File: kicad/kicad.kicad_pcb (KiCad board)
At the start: 2 copper layers, 86.4 x 53.3 mm, 12 parts, among them J1 Conn_01x06_Male, J2 Conn_01x02_Male, J3 Conn_01x02_Male, U1 4Bit_China_Level_Shifter, U2 WeMos_D1_mini, U3 LTV-817

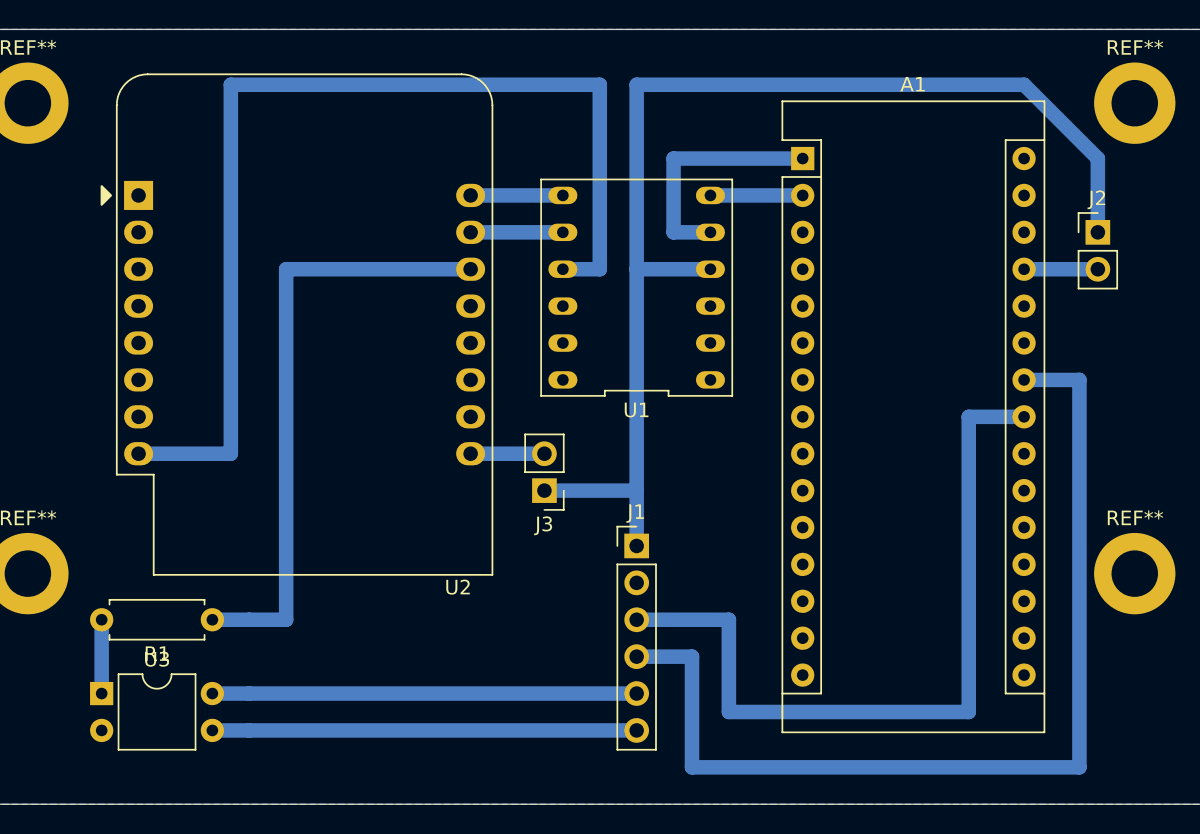
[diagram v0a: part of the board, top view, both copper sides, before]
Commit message: make thicker wires to make soldering of routed pcbs easier
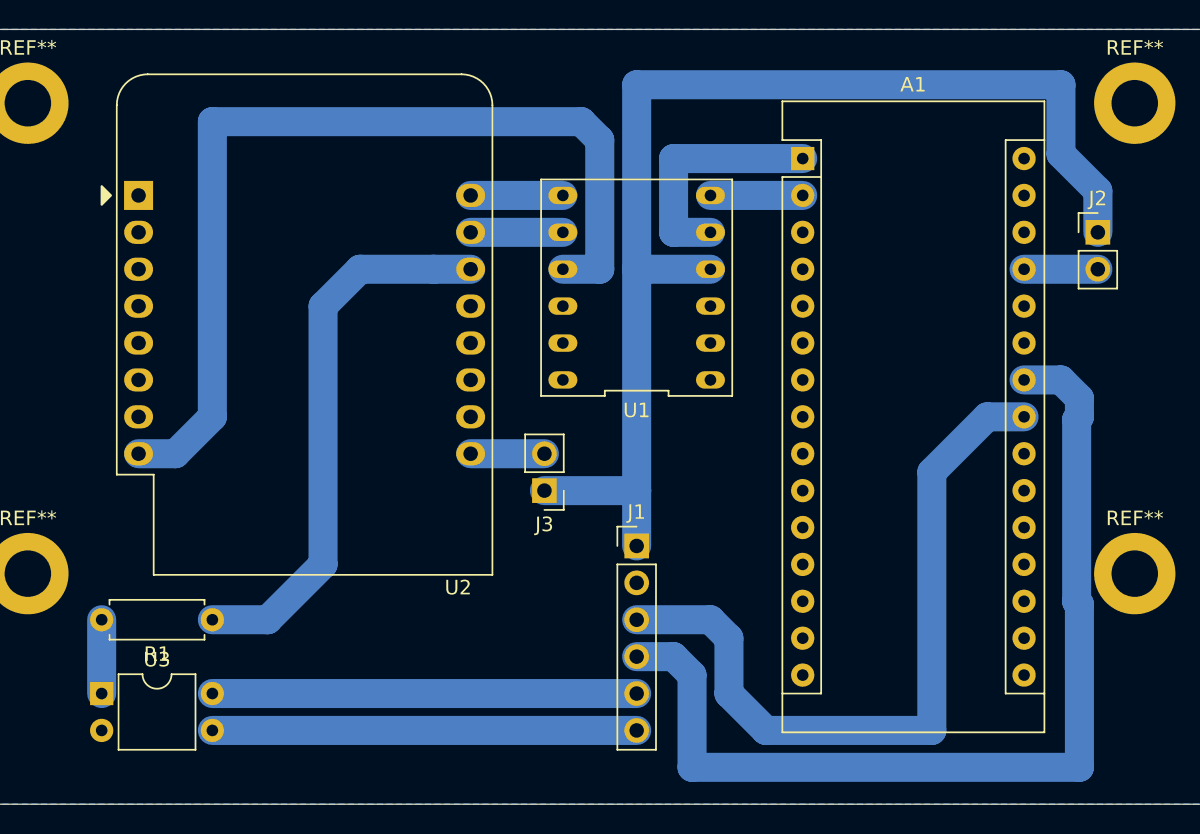
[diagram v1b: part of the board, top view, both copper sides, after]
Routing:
- net Net-(U1-Pad9): track 72.4 -> 65.1 mm
- net Net-(R1-Pad1): track 41.9 -> 38.2 mm
- net SDA: track 53.3 -> 51.4 mm
- net VCC: track 82.1 -> 83.6 mm
- net SCL: track 68.6 -> 67.2 mm
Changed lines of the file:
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@@
     (thickness 1.6)
     (drawings 4)
-    (tracks 40)
+    (tracks 52)
     (zones 0)
     (modules 12)
@@
   )
   (setup
-    (last_trace_width 1)
+    (last_trace_width 2)
     (user_trace_width 1)
+    (user_trace_width 2)
     (trace_clearance 0.2)
     (zone_clearance 0.508)
@@
   (gr_line (start 134.62 48.26) (end 134.62 101.6) (layer Edge.Cuts) (width 0.05))
   (gr_line (start 48.26 48.26) (end 134.62 48.26) (layer Edge.Cuts) (width 0.05))
-  (segment (start 100.33 62.23) (end 97.79 62.23) (width 1) (layer B.Cu) (net 1))
-  (segment (start 97.79 62.23) (end 97.79 57.15) (width 1) (layer B.Cu) (net 1))
-  (segment (start 97.79 57.15) (end 106.68 57.15) (width 1) (layer B.Cu) (net 1))
-  (segment (start 100.33 59.69) (end 106.68 59.69) (width 1) (layer B.Cu) (net 3))
-  (segment (start 118.11 74.93) (end 121.92 74.93) (width 1) (layer B.Cu) (net 13))
-  (segment (start 118.11 95.25) (end 118.11 74.93) (width 1) (layer B.Cu) (net 13))
-  (segment (start 101.6 95.25) (end 118.11 95.25) (width 1) (layer B.Cu) (net 13))
-  (segment (start 101.6 88.9) (end 101.6 95.25) (width 1) (layer B.Cu) (net 13))
-  (segment (start 95.25 88.9) (end 101.6 88.9) (width 1) (layer B.Cu) (net 13))
-  (segment (start 125.73 72.39) (end 121.92 72.39) (width 1) (layer B.Cu) (net 14))
-  (segment (start 125.73 99.06) (end 125.73 72.39) (width 1) (layer B.Cu) (net 14))
-  (segment (start 99.06 99.06) (end 125.73 99.06) (width 1) (layer B.Cu) (net 14))
-  (segment (start 99.06 91.44) (end 99.06 99.06) (width 1) (layer B.Cu) (net 14))
-  (segment (start 95.25 91.44) (end 99.06 91.44) (width 1) (layer B.Cu) (net 14))
-  (segment (start 127 64.77) (end 121.92 64.77) (width 1) (layer B.Cu) (net 20))
-  (segment (start 88.9 80.01) (end 95.25 80.01) (width 1) (layer B.Cu) (net 28))
-  (segment (start 95.25 80.01) (end 95.25 83.82) (width 1) (layer B.Cu) (net 28))
-  (segment (start 95.25 52.07) (end 121.92 52.07) (width 1) (layer B.Cu) (net 28))
-  (segment (start 121.92 52.07) (end 127 57.15) (width 1) (layer B.Cu) (net 28))
-  (segment (start 127 57.15) (end 127 62.23) (width 1) (layer B.Cu) (net 28))
-  (segment (start 95.25 64.77) (end 100.33 64.77) (width 1) (layer B.Cu) (net 28))
-  (segment (start 95.25 80.01) (end 95.25 64.77) (width 1) (layer B.Cu) (net 28))
-  (segment (start 95.25 64.77) (end 95.25 52.07) (width 1) (layer B.Cu) (net 28))
-  (segment (start 68.58 93.98) (end 95.25 93.98) (width 1) (layer B.Cu) (net 29))
-  (segment (start 68.58 93.98) (end 66.04 93.98) (width 1) (layer B.Cu) (net 29))
-  (segment (start 68.58 96.52) (end 95.25 96.52) (width 1) (layer B.Cu) (net 30))
-  (segment (start 68.58 96.52) (end 66.04 96.52) (width 1) (layer B.Cu) (net 30))
-  (segment (start 83.82 77.47) (end 88.9 77.47) (width 1) (layer B.Cu) (net 31))
-  (segment (start 68.58 88.9) (end 71.12 88.9) (width 1) (layer B.Cu) (net 32))
-  (segment (start 71.12 88.9) (end 71.12 64.77) (width 1) (layer B.Cu) (net 32))
-  (segment (start 71.12 64.77) (end 83.82 64.77) (width 1) (layer B.Cu) (net 32))
-  (segment (start 68.58 88.9) (end 66.04 88.9) (width 1) (layer B.Cu) (net 32))
-  (segment (start 58.42 88.9) (end 58.42 93.98) (width 1) (layer B.Cu) (net 33))
-  (segment (start 90.17 64.77) (end 92.71 64.77) (width 1) (layer B.Cu) (net 38))
-  (segment (start 92.71 64.77) (end 92.71 52.07) (width 1) (layer B.Cu) (net 38))
-  (segment (start 92.71 52.07) (end 67.31 52.07) (width 1) (layer B.Cu) (net 38))
-  (segment (start 67.31 52.07) (end 67.31 77.47) (width 1) (layer B.Cu) (net 38))
-  (segment (start 67.31 77.47) (end 60.96 77.47) (width 1) (layer B.Cu) (net 38))
-  (segment (start 90.17 62.23) (end 83.82 62.23) (width 1) (layer B.Cu) (net 39))
-  (segment (start 90.17 59.69) (end 83.82 59.69) (width 1) (layer B.Cu) (net 40))
+  (segment (start 100.33 62.23) (end 97.79 62.23) (width 2) (layer B.Cu) (net 1))
+  (segment (start 97.79 62.23) (end 97.79 57.15) (width 2) (layer B.Cu) (net 1))
+  (segment (start 97.79 57.15) (end 106.68 57.15) (width 2) (layer B.Cu) (net 1))
+  (segment (start 100.33 59.69) (end 106.68 59.69) (width 2) (layer B.Cu) (net 3))
+  (segment (start 119.38 74.93) (end 121.92 74.93) (width 2) (layer B.Cu) (net 13))
+  (segment (start 115.57 78.74) (end 119.38 74.93) (width 2) (layer B.Cu) (net 13))
+  (segment (start 104.14 96.52) (end 115.57 96.52) (width 2) (layer B.Cu) (net 13))
+  (segment (start 101.6 93.98) (end 104.14 96.52) (width 2) (layer B.Cu) (net 13))
+  (segment (start 100.33 88.9) (end 101.6 90.17) (width 2) (layer B.Cu) (net 13))
+  (segment (start 115.57 96.52) (end 115.57 78.74) (width 2) (layer B.Cu) (net 13))
+  (segment (start 101.6 90.17) (end 101.6 93.98) (width 2) (layer B.Cu) (net 13))
+  (segment (start 95.25 88.9) (end 100.33 88.9) (width 2) (layer B.Cu) (net 13))
+  (segment (start 95.25 91.44) (end 97.79 91.44) (width 2) (layer B.Cu) (net 14))
+  (segment (start 121.92 72.39) (end 124.46 72.39) (width 2) (layer B.Cu) (net 14))
+  (segment (start 97.79 91.44) (end 99.06 92.71) (width 2) (layer B.Cu) (net 14))
+  (segment (start 99.06 92.71) (end 99.06 99.06) (width 2) (layer B.Cu) (net 14))
+  (segment (start 99.06 99.06) (end 125.73 99.06) (width 2) (layer B.Cu) (net 14))
+  (segment (start 125.539999 87.645001) (end 125.539999 75.120001) (width 2) (layer B.Cu) (net 14))
+  (segment (start 125.73 87.835002) (end 125.539999 87.645001) (width 2) (layer B.Cu) (net 14))
+  (segment (start 125.73 99.06) (end 125.73 87.835002) (width 2) (layer B.Cu) (net 14))
+  (segment (start 125.539999 75.120001) (end 125.73 74.93) (width 2) (layer B.Cu) (net 14))
+  (segment (start 125.73 73.66) (end 124.46 72.39) (width 2) (layer B.Cu) (net 14))
+  (segment (start 125.73 74.93) (end 125.73 73.66) (width 2) (layer B.Cu) (net 14))
+  (segment (start 127 64.77) (end 121.92 64.77) (width 2) (layer B.Cu) (net 20))
+  (segment (start 88.9 80.01) (end 95.25 80.01) (width 2) (layer B.Cu) (net 28))
+  (segment (start 95.25 83.82) (end 95.25 80.01) (width 2) (layer B.Cu) (net 28))
+  (segment (start 100.33 64.77) (end 95.25 64.77) (width 2) (layer B.Cu) (net 28))
+  (segment (start 95.25 64.77) (end 95.25 52.07) (width 2) (layer B.Cu) (net 28))
+  (segment (start 95.25 80.01) (end 95.25 64.77) (width 2) (layer B.Cu) (net 28))
+  (segment (start 127 59.38) (end 124.46 56.84) (width 2) (layer B.Cu) (net 28))
+  (segment (start 127 62.23) (end 127 59.38) (width 2) (layer B.Cu) (net 28))
+  (segment (start 124.46 56.84) (end 124.46 52.07) (width 2) (layer B.Cu) (net 28))
+  (segment (start 124.46 52.07) (end 95.25 52.07) (width 2) (layer B.Cu) (net 28))
+  (segment (start 66.04 93.98) (end 95.25 93.98) (width 2) (layer B.Cu) (net 29))
+  (segment (start 66.04 96.52) (end 95.25 96.52) (width 2) (layer B.Cu) (net 30))
+  (segment (start 83.82 77.47) (end 88.9 77.47) (width 2) (layer B.Cu) (net 31))
+  (segment (start 76.2 64.77) (end 81.28 64.77) (width 2) (layer B.Cu) (net 32))
+  (segment (start 73.66 67.31) (end 76.2 64.77) (width 2) (layer B.Cu) (net 32))
+  (segment (start 81.28 64.77) (end 83.82 64.77) (width 2) (layer B.Cu) (net 32))
+  (segment (start 73.66 85.09) (end 73.66 67.31) (width 2) (layer B.Cu) (net 32))
+  (segment (start 69.85 88.9) (end 73.66 85.09) (width 2) (layer B.Cu) (net 32))
+  (segment (start 66.04 88.9) (end 69.85 88.9) (width 2) (layer B.Cu) (net 32))
+  (segment (start 58.42 88.9) (end 58.42 93.98) (width 2) (layer B.Cu) (net 33))
+  (segment (start 63.5 77.47) (end 60.96 77.47) (width 2) (layer B.Cu) (net 38))
+  (segment (start 92.71 55.88) (end 91.44 54.61) (width 2) (layer B.Cu) (net 38))
+  (segment (start 92.71 64.77) (end 92.71 55.88) (width 2) (layer B.Cu) (net 38))
+  (segment (start 66.04 74.93) (end 63.5 77.47) (width 2) (layer B.Cu) (net 38))
+  (segment (start 66.04 54.61) (end 66.04 74.93) (width 2) (layer B.Cu) (net 38))
+  (segment (start 91.44 54.61) (end 66.04 54.61) (width 2) (layer B.Cu) (net 38))
+  (segment (start 90.17 64.77) (end 92.71 64.77) (width 2) (layer B.Cu) (net 38))
+  (segment (start 83.82 62.23) (end 90.17 62.23) (width 2) (layer B.Cu) (net 39))
+  (segment (start 90.17 59.69) (end 83.82 59.69) (width 2) (layer B.Cu) (net 40))
   (zone (net 7) (net_name GND) (layer B.Cu) (hatch edge 0.508)
     (connect_pads (clearance 0.508))

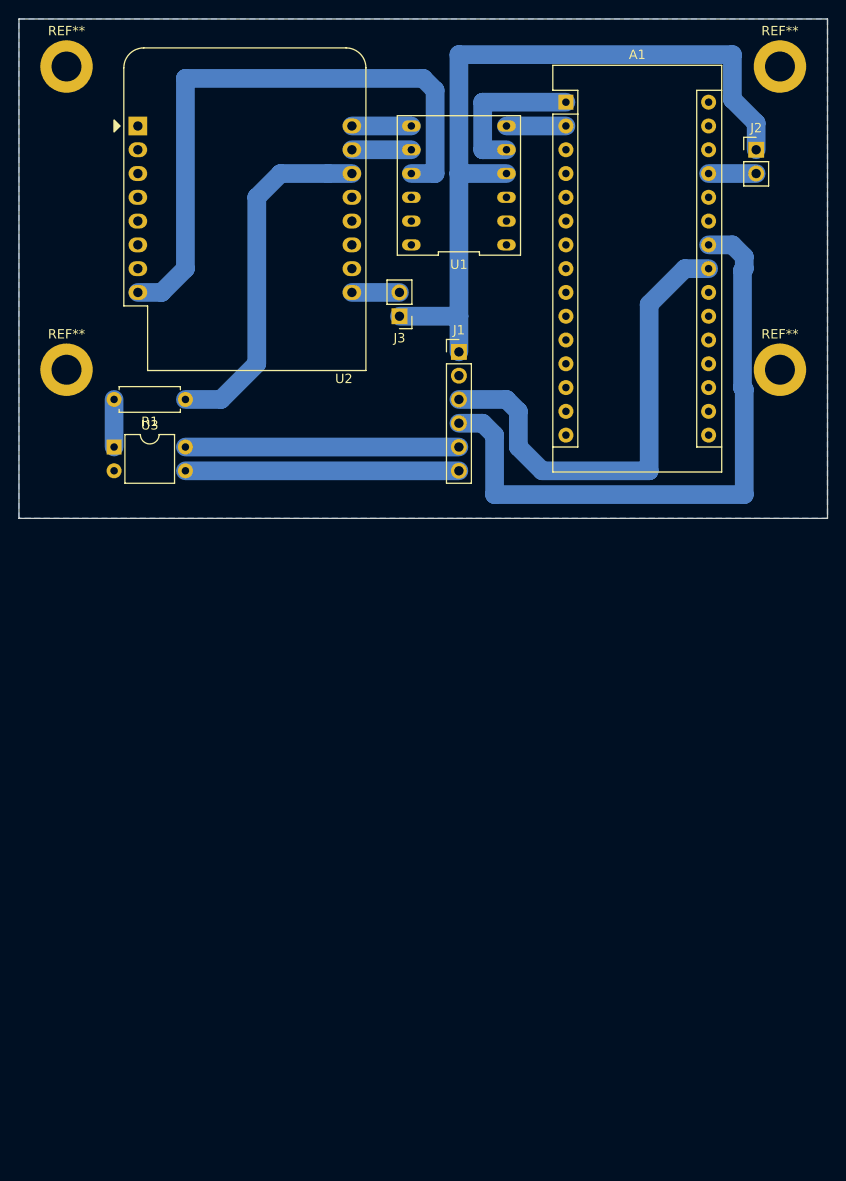
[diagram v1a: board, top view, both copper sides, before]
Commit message: add output to switch an external relay with an external voltage
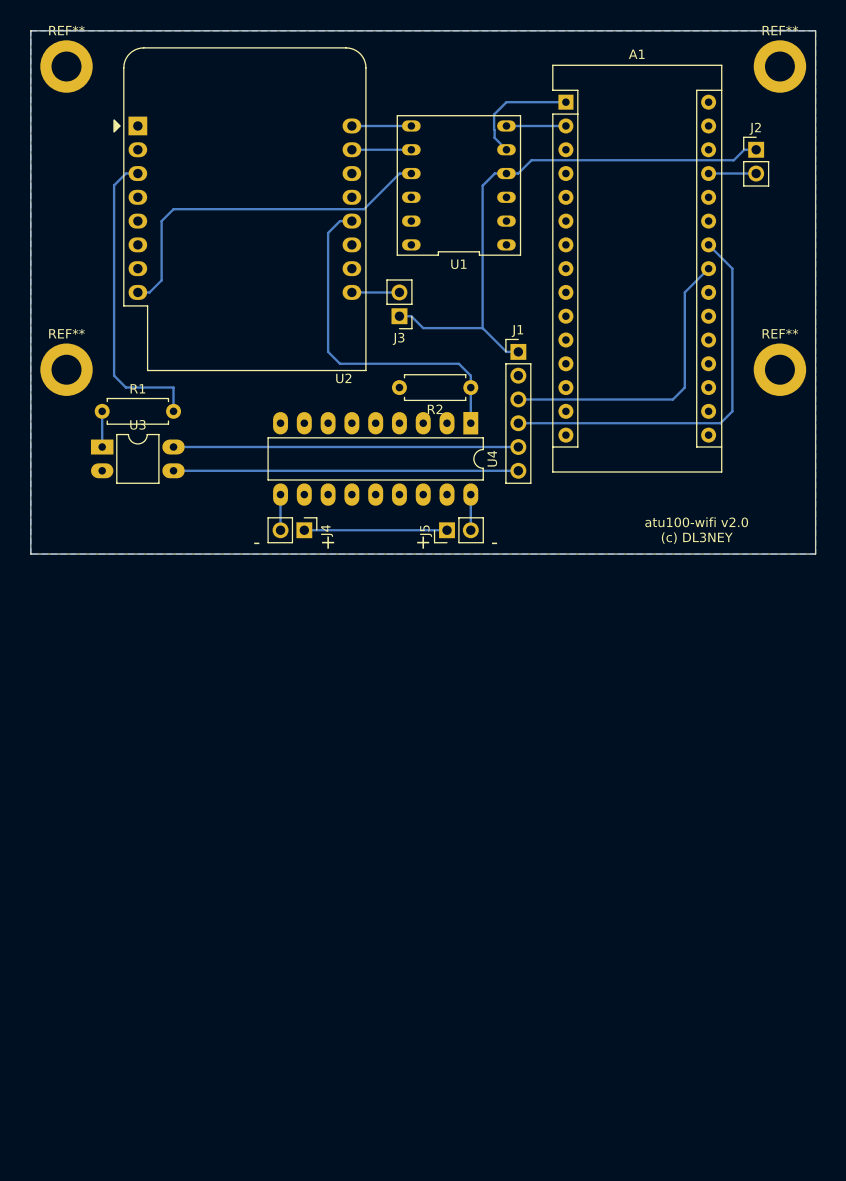
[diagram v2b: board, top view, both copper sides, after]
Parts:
- added J4: 12V, Connector_PinHeader_2.54mm:PinHeader_1x02_P2.54mm_Vertical, F.Cu at (78.7, 102.9)
- added J5: Relay Switch, Connector_PinHeader_2.54mm:PinHeader_1x02_P2.54mm_Vertical, F.Cu at (94.0, 102.9)
- added R2: 10k, Resistor_THT:R_Axial_DIN0207_L6.3mm_D2.5mm_P7.62mm_Horizontal, F.Cu at (96.5, 87.6)
- added U4: ULN2803A, Package_DIP:DIP-18_W7.62mm_LongPads, F.Cu at (96.5, 91.4)
- U3: footprint Package_DIP:DIP-4_W7.62mm -> Package_DIP:DIP-4_W7.62mm_LongPads
- moved R1 8.98 mm to (57.1, 90.2), turned to 0 degrees
- moved J1 6.35 mm to (101.6, 83.8)
- moved U3 1.27 mm to (57.1, 94.0)
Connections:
- U2 pad 14: Net-(R1-Pad1) -> Net-(U2-Pad14)
- U2 pad 3: Net-(U2-Pad3) -> Net-(R1-Pad2)
- U3 pad 1: Net-(R1-Pad2) -> Net-(R1-Pad1)
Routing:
- net Net-(R2-Pad1): track 0.00 -> 37.1 mm
- net Net-(R1-Pad1): track 38.2 -> 3.81 mm
- net Net-(R1-Pad2): track 5.08 -> 32.8 mm
- net Net-(U1-Pad9): track 65.1 -> 38.2 mm
- net SCL: track 67.2 -> 42.2 mm
- net VCC: track 83.6 -> 60.3 mm
- net SDA: track 51.4 -> 32.1 mm
- net Net-(J4-Pad1): track 0.00 -> 15.2 mm
- net BTN-: track 29.2 -> 36.8 mm
- net BTN+: track 29.2 -> 36.8 mm
- net Net-(A1-Pad1): track 16.5 -> 12.5 mm
- net Net-(J5-Pad2): track 0.00 -> 3.81 mm
- net Net-(J4-Pad2): track 0.00 -> 3.81 mm
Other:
- board size 86.4 x 53.3 mm -> 83.8 x 55.9 mm
- board text added: "+"
- board text added: "-"
- board text added: "atu100-wifi v2.0 (c) DL3NEY"
